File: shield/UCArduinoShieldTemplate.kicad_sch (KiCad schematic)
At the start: 16 parts, among them J1 Conn_02x05_Counter_Clockwise, J3 Conn_02x05_Counter_Clockwise, P1 Power, P2 Analog, P3 Digital, P4 Digital, SW1 UC_SW_Push, SW2 UC_SW_Push

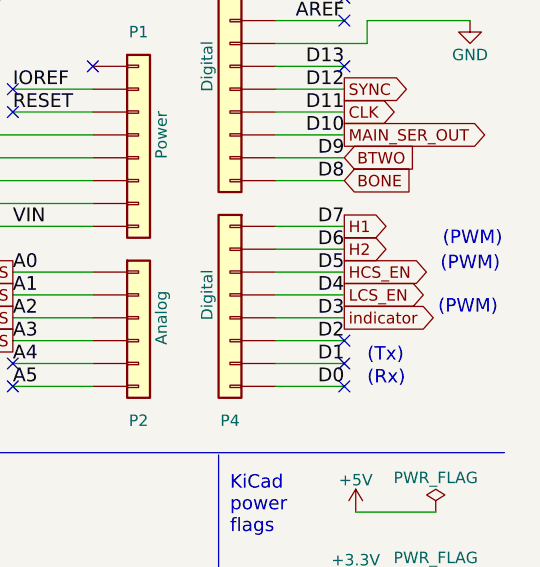
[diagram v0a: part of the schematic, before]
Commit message: added the unos code
added what should be a basic working version of the arduino unos code.
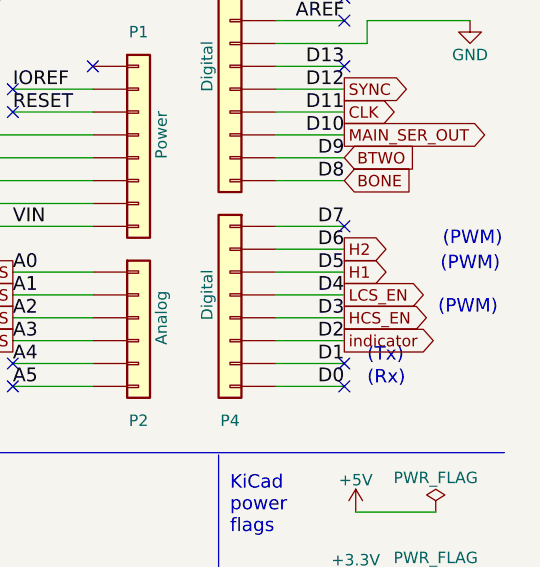
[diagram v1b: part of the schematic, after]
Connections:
- net D2 is gone; now on net indicator: P4.6 (Pin_6)
- net H1: now also P4.3 (Pin_3); no longer P4.1 (Pin_1)
- net HCS_EN: now also P4.5 (Pin_5); no longer P4.3 (Pin_3)
- net indicator: no longer P4.5 (Pin_5)
- new net D7: P4.1 (Pin_1)
